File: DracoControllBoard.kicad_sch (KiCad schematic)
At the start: 21 parts, among them SW1 SW_Push, SW10 SW_Push, SW11 SW_Push, SW12 SW_Push, SW2 SW_Push, SW3 SW_Push, SW4 SW_Push, SW5 SW_Push, SW6 SW_Push, SW7 SW_Push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

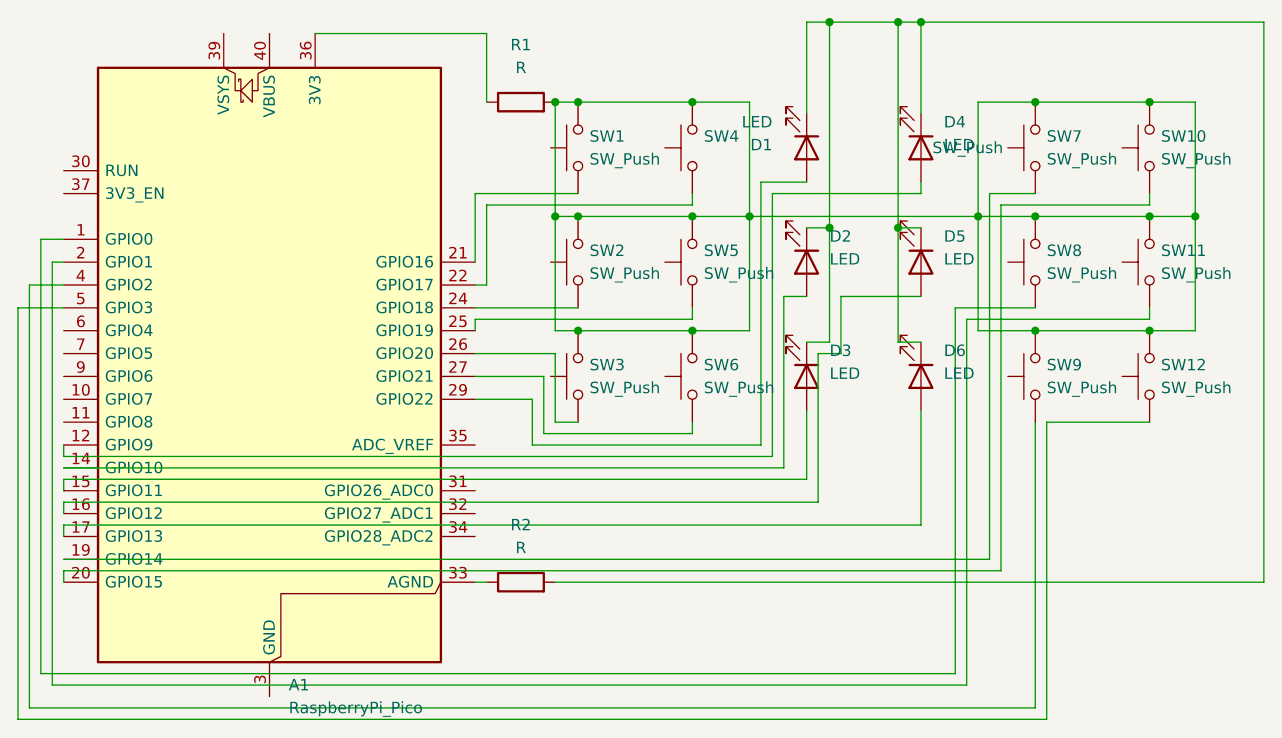
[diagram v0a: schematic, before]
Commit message: fixted resistor issues
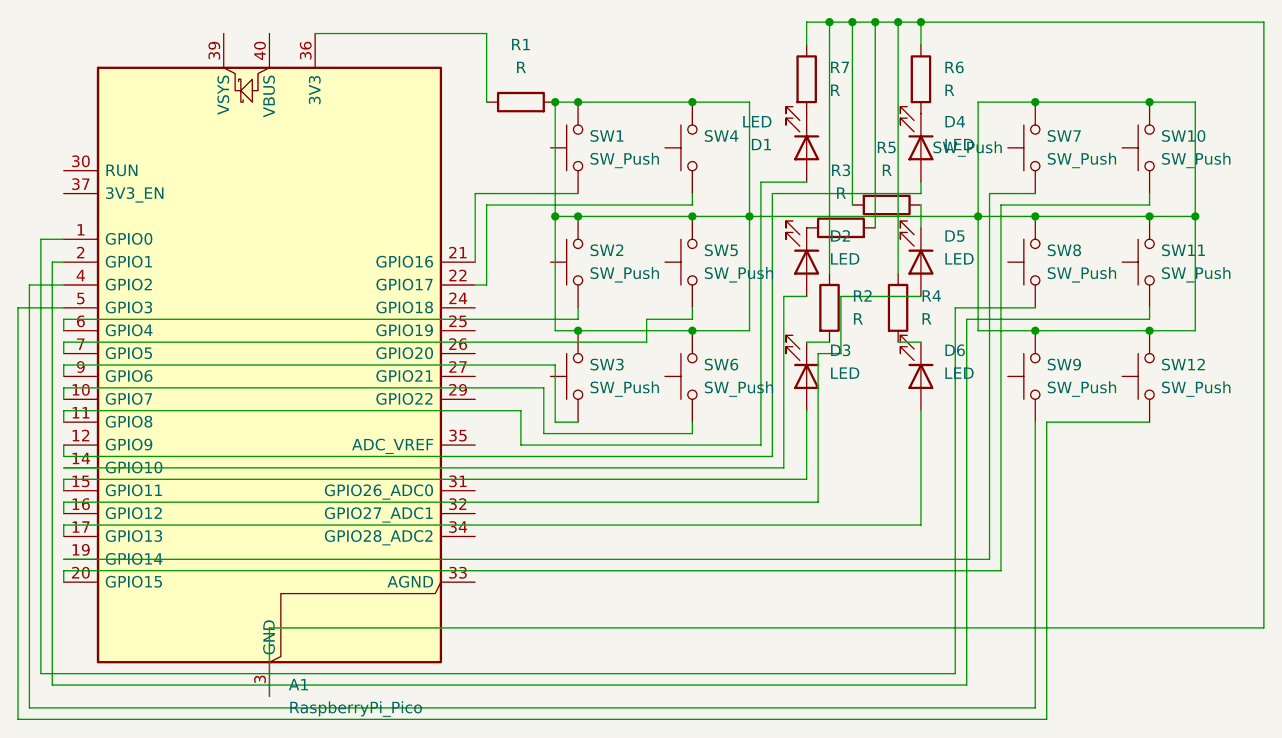
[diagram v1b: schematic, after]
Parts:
- added R3, R4, R5, R6, R7: R, Resistor_THT:R_Axial_DIN0207_L6.3mm_D2.5mm_P7.62mm_Horizontal, symbol Device:R
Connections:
- net at SW5.1: now also A1.7 (GPIO5); no longer A1.25 (GPIO19)
- net at A1.10 (GPIO7): now also SW6.1
- net at A1.11 (GPIO8): now also D1.2 (A)
- net at A1.13 (GND), A1.18 (GND), A1.23 (GND)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: now also R2.1, R3.2, R4.1, R5.2, R6.1, R7.1
- net at A1.24 (GPIO18): no longer SW2.1
- net at A1.26 (GPIO20): no longer SW3.1
- net at A1.27 (GPIO21): no longer SW6.1
- net at A1.29 (GPIO22): no longer D1.2 (A)
- net at A1.33 (AGND): no longer R2.1
- net at A1.6 (GPIO4): now also SW2.1
- net at A1.9 (GPIO6): now also SW3.1
- new net: D2.1 (K), R3.1
- new net: D4.1 (K), R6.2
- new net: D5.1 (K), R5.1
- new net: D3.1 (K), R2.2
- new net: D1.1 (K), R7.2
- new net: D6.1 (K), R4.2
